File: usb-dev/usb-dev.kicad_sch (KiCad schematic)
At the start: 42 parts, among them J1 HS USB, J2 FS USB, J3 Conn_02x05_Odd_Even, J4 Conn_02x05_Odd_Even, J5 Molex_104031-0811, J6 Conn_01x06_Male, SW1 SW_Push, SW2 SW_Push, SW3 SW_Push, U1 LPC55x16JEV98E, U2 AP2127K-3.3, Y1 ABM8-16.000MHZ-B2-T

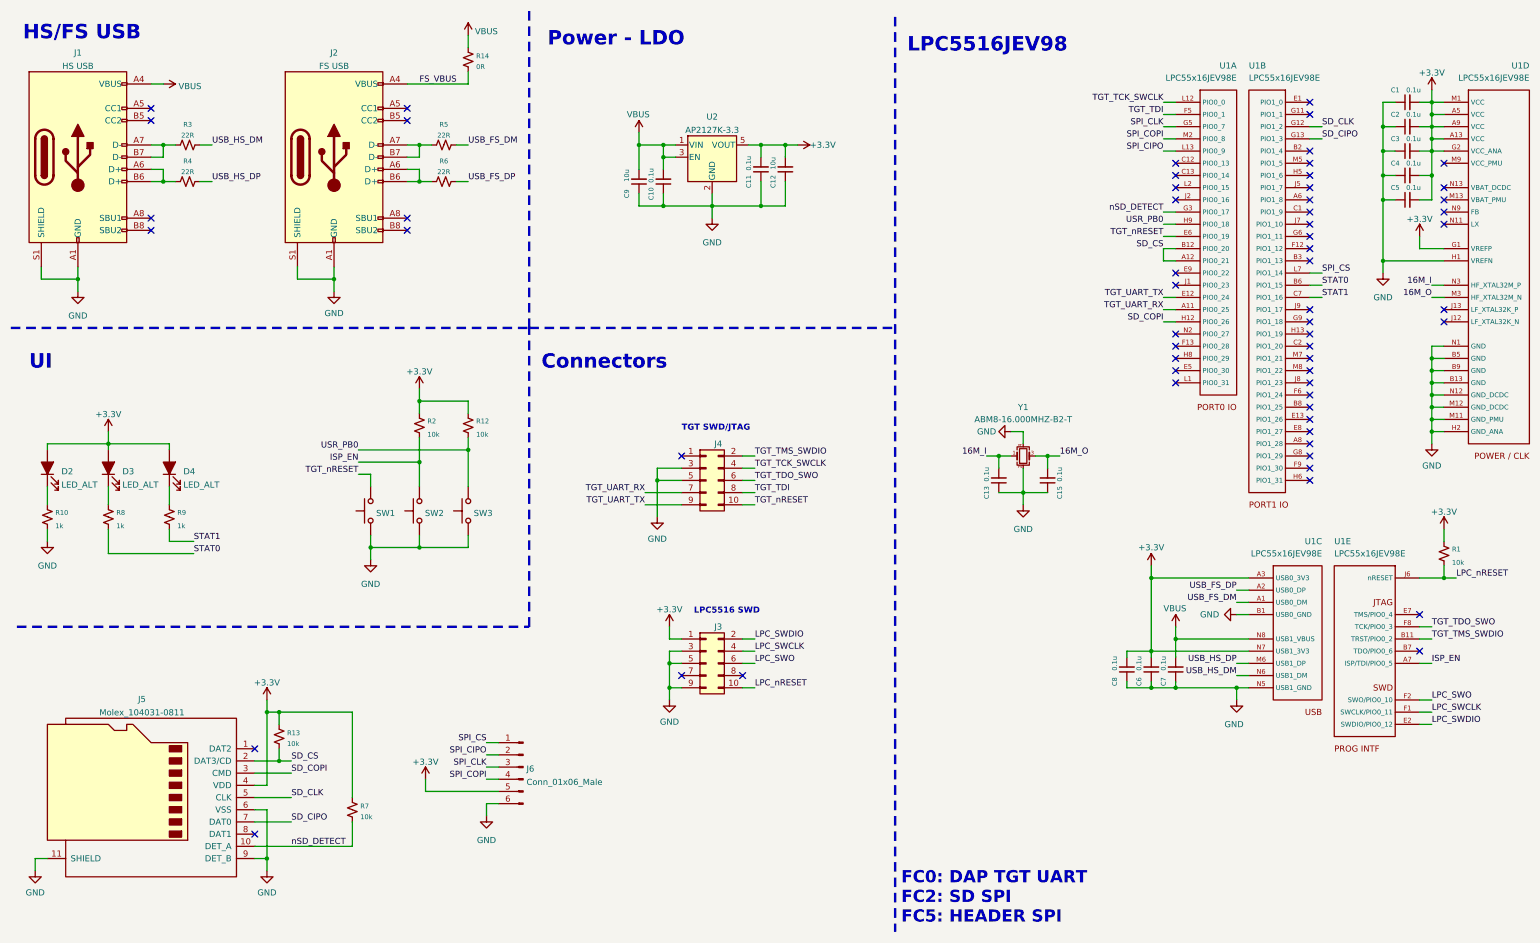
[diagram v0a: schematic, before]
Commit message: Fixed VDD_PMU, added fet to SD power and added extra CS line to SPI header
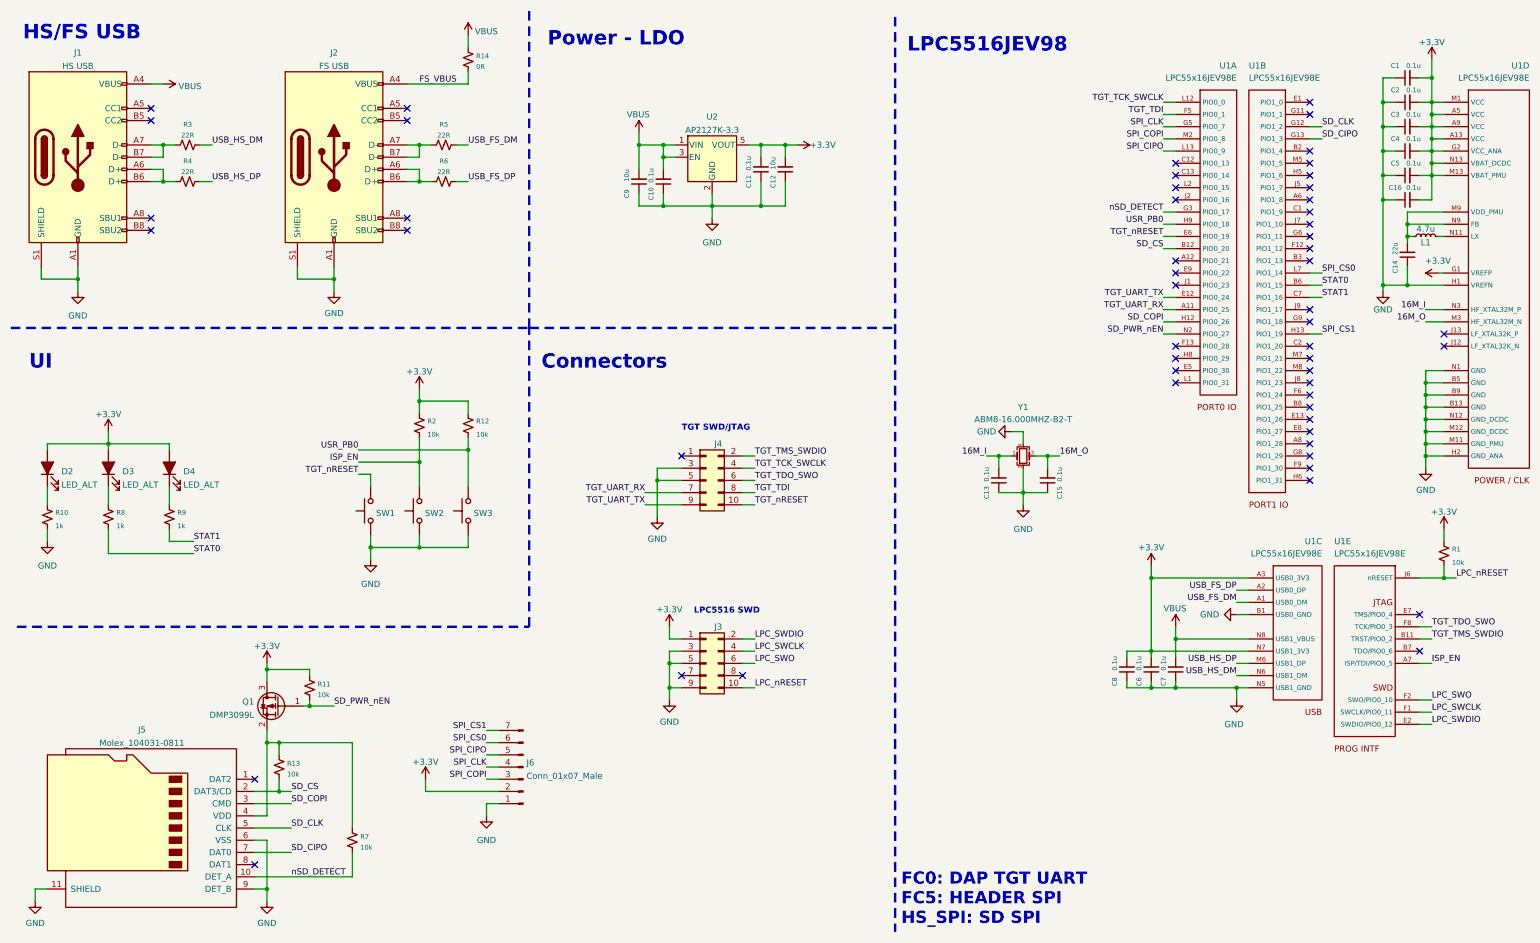
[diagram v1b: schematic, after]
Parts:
- removed J6: Conn_01x06_Male, Connector_PinHeader_2.54mm:PinHeader_1x06_P2.54mm_Vertical, symbol Connector:Conn_01x06_Male
- added C14: 22u, Capacitor_SMD:C_0402_1005Metric, symbol Device:C_Small
- added C16: 0.1u, Capacitor_SMD:C_0402_1005Metric, symbol Device:C_Small
- added J6: Conn_01x07_Male, Connector_PinHeader_2.54mm:PinHeader_1x07_P2.54mm_Vertical, symbol Connector:Conn_01x07_Male
- added L1: 4.7u, Inductor_SMD:L_0805_2012Metric, symbol Device:L_Small
- added Q1: DMP3099L, Package_TO_SOT_SMD:SOT-23, symbol Device:Q_PMOS_GSD
- added R11: 10k, Resistor_SMD:R_0402_1005Metric, symbol Device:R_Small_US
- J3, J4: footprint Connector_PinHeader_1.00mm:PinHeader_2x05_P1.00mm_Vertical_SMD -> Connector_PinHeader_1.27mm:PinHeader_2x05_P1.27mm_Vertical_SMD
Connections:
- net +3V3: now also U1.M13 (VBAT_PMU), U1.N13 (VBAT_DCDC), C16.2, J6.2 (Pin_2), Q1.3 (D), R11.2; no longer J5.4 (VDD), R13.2, R7.2
- net GND: now also C14.1, C16.1, J6.1 (Pin_1)
- net SD_CS: no longer U1.A12 (PIO0_21)
- net SPI_CIPO: now also J6.5 (Pin_5)
- net SPI_CLK: now also J6.4 (Pin_4)
- net SPI_COPI: now also J6.3 (Pin_3)
- net SD_PWR_nEN: now reaches U1.N2 (PIO0_27)
- net SD_PWR_nEN: now also Q1.1 (G), R11.1
- net at U1.M9 (VDD_PMU): now also U1.N9 (FB), C14.2, L1.1
- net at U1.N11 (LX): now also L1.2
- net SPI_CS1: now reaches U1.H13 (PIO1_19)
- net SPI_CS1: now also J6.7 (Pin_7)
- net SPI_CS renamed SPI_CS0
- net SPI_CS0: now also J6.6 (Pin_6)
- new net: J5.4 (VDD), Q1.2 (S), R13.2, R7.2
- no-connect marks 60 -> 54
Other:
- note added: "FC0: DAP TGT UART FC5: HEADER SPI HS_SPI: SD SPI"
- note removed: "FC0: DAP TGT UART FC2: SD SPI FC5: HEADER SPI"
- moved on the sheet: C1, C2, C3, C4, C5, J5, R13, R7, U1D

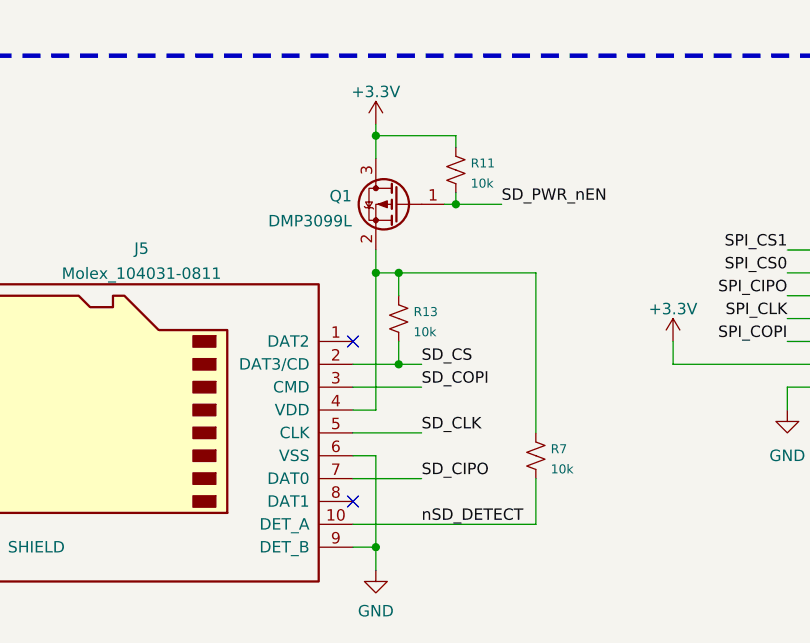
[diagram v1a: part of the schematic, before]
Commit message: Fixed missing VDDCORE connections to internal switcher D:
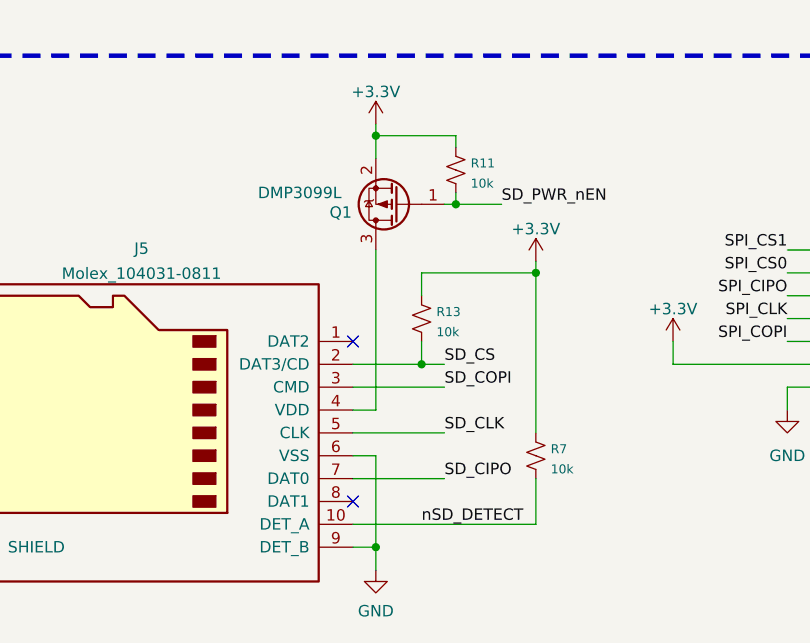
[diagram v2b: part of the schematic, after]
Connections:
- net +3V3: now also Q1.2 (S), R13.2, R7.2; no longer Q1.3 (D)
- new net: J5.4 (VDD), Q1.3 (D)
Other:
- moved on the sheet: Q1, R13
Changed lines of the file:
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@@
   (junction (at 43.18 39.37) (diameter 0) (color 0 0 0 0)
   )
-  (junction (at 67.31 163.83) (diameter 0) (color 0 0 0 0)
-  )
   (junction (at 157.48 52.07) (diameter 0) (color 0 0 0 0)
   )
@@
   (junction (at 222.25 111.76) (diameter 0) (color 0 0 0 0)
   )
-  (junction (at 67.31 173.99) (diameter 0) (color 0 0 0 0)
+  (junction (at 69.85 173.99) (diameter 0) (color 0 0 0 0)
   )
   (junction (at 106.68 102.87) (diameter 0) (color 0 0 0 0)
   )
+  (junction (at 64.77 148.59) (diameter 0) (color 0 0 0 0)
+  )
   (junction (at 148.59 152.4) (diameter 0) (color 0 0 0 0)
   )
   (junction (at 96.52 92.71) (diameter 0) (color 0 0 0 0)
   )
+  (junction (at 73.66 156.21) (diameter 0) (color 0 0 0 0)
+  )
   (junction (at 25.4 67.31) (diameter 0) (color 0 0 0 0)
   )
@@
   (junction (at 307.34 35.56) (diameter 0) (color 0 0 0 0)
   )
-  (junction (at 64.77 148.59) (diameter 0) (color 0 0 0 0)
-  )
   (junction (at 146.05 109.22) (diameter 0) (color 0 0 0 0)
   )
@@
   (junction (at 297.18 40.64) (diameter 0) (color 0 0 0 0)
   )
+  (junction (at 82.55 163.83) (diameter 0) (color 0 0 0 0)
+  )
   (junction (at 307.34 40.64) (diameter 0) (color 0 0 0 0)
   )
   (junction (at 227.33 104.14) (diameter 0) (color 0 0 0 0)
   )
-  (junction (at 64.77 163.83) (diameter 0) (color 0 0 0 0)
-  )
   (junction (at 96.52 46.99) (diameter 0) (color 0 0 0 0)
   )
@@
   )
   (junction (at 307.34 30.48) (diameter 0) (color 0 0 0 0)
-  )
-  (junction (at 73.66 156.21) (diameter 0) (color 0 0 0 0)
   )
   (junction (at 248.92 129.54) (diameter 0) (color 0 0 0 0)
@@
   (no_connect (at 62.23 189.23))
   (no_connect (at 163.83 149.86))
-  (wire (pts (xy 67.31 173.99) (xy 69.85 173.99))
+  (wire (pts (xy 69.85 173.99) (xy 72.39 173.99))
     (stroke (width 0) (type default) (color 0 0 0 0))
   )
@@
     (stroke (width 0) (type default) (color 0 0 0 0))
   )
-  (wire (pts (xy 67.31 163.83) (xy 64.77 163.83))
-    (stroke (width 0) (type default) (color 0 0 0 0))
-  )
   (wire (pts (xy 307.34 45.72) (xy 307.34 43.18))
     (stroke (width 0) (type default) (color 0 0 0 0))
@@
     (stroke (width 0.5) (type dash_dot) (color 0 0 0 0))
   )
+  (wire (pts (xy 82.55 162.56) (xy 82.55 163.83))
+    (stroke (width 0) (type default) (color 0 0 0 0))
+  )
   (wire (pts (xy 157.48 49.53) (xy 157.48 52.07))
     (stroke (width 0) (type default) (color 0 0 0 0))
@@
     (stroke (width 0) (type default) (color 0 0 0 0))
   )
-  (wire (pts (xy 67.31 163.83) (xy 82.55 163.83))
+  (wire (pts (xy 69.85 163.83) (xy 82.55 163.83))
     (stroke (width 0) (type default) (color 0 0 0 0))
   )
@@
   )
   (wire (pts (xy 302.26 68.58) (xy 297.18 68.58))
+    (stroke (width 0) (type default) (color 0 0 0 0))
+  )
+  (wire (pts (xy 72.39 156.21) (xy 73.66 156.21))
     (stroke (width 0) (type default) (color 0 0 0 0))
   )
@@
     (stroke (width 0) (type default) (color 0 0 0 0))
   )
-  (wire (pts (xy 67.31 171.45) (xy 67.31 173.99))
+  (wire (pts (xy 69.85 171.45) (xy 69.85 173.99))
     (stroke (width 0) (type default) (color 0 0 0 0))
   )
@@
   )
   (wire (pts (xy 304.8 45.72) (xy 307.34 45.72))
-    (stroke (width 0) (type default) (color 0 0 0 0))
-  )
-  (wire (pts (xy 64.77 161.29) (xy 64.77 163.83))
     (stroke (width 0) (type default) (color 0 0 0 0))
   )
@@
     (stroke (width 0) (type default) (color 0 0 0 0))
   )
+  (wire (pts (xy 64.77 148.59) (xy 64.77 151.13))
+    (stroke (width 0) (type default) (color 0 0 0 0))
+  )
   (wire (pts (xy 64.77 148.59) (xy 73.66 148.59))
     (stroke (width 0) (type default) (color 0 0 0 0))
   )
   (wire (pts (xy 104.14 39.37) (xy 106.68 39.37))
-    (stroke (width 0) (type default) (color 0 0 0 0))
-  )
-  (wire (pts (xy 72.39 156.21) (xy 73.66 156.21))
     (stroke (width 0) (type default) (color 0 0 0 0))
   )
@@
     (stroke (width 0) (type default) (color 0 0 0 0))
   )
-  (wire (pts (xy 62.23 186.69) (xy 69.85 186.69))
+  (wire (pts (xy 62.23 186.69) (xy 72.39 186.69))
     (stroke (width 0) (type default) (color 0 0 0 0))
   )
@@
     (stroke (width 0) (type default) (color 0 0 0 0))
   )
-  (wire (pts (xy 64.77 148.59) (xy 64.77 151.13))
-    (stroke (width 0) (type default) (color 0 0 0 0))
-  )
   (wire (pts (xy 96.52 92.71) (xy 106.68 92.71))
     (stroke (width 0) (type default) (color 0 0 0 0))
@@
     (stroke (width 0) (type default) (color 0 0 0 0))
   )
-  (wire (pts (xy 64.77 163.83) (xy 64.77 179.07))
-    (stroke (width 0) (type default) (color 0 0 0 0))
-  )
   (wire (pts (xy 243.84 151.13) (xy 243.84 152.4))
     (stroke (width 0) (type default) (color 0 0 0 0))
@@
     (stroke (width 0) (type default) (color 0 0 0 0))
   )
-  (wire (pts (xy 67.31 166.37) (xy 67.31 163.83))
+  (wire (pts (xy 69.85 166.37) (xy 69.85 163.83))
     (stroke (width 0) (type default) (color 0 0 0 0))
   )
@@
     (stroke (width 0) (type default) (color 0 0 0 0))
   )
+  (wire (pts (xy 64.77 161.29) (xy 64.77 179.07))
+    (stroke (width 0) (type default) (color 0 0 0 0))
+  )
   (wire (pts (xy 307.34 33.02) (xy 309.88 33.02))
     (stroke (width 0) (type default) (color 0 0 0 0))
@@
     (stroke (width 0) (type default) (color 0 0 0 0))
   )
-  (wire (pts (xy 62.23 176.53) (xy 69.85 176.53))
+  (wire (pts (xy 62.23 176.53) (xy 72.39 176.53))
     (stroke (width 0) (type default) (color 0 0 0 0))
   )
@@
     (stroke (width 0) (type default) (color 0 0 0 0))
   )
-  (wire (pts (xy 62.23 173.99) (xy 67.31 173.99))
+  (wire (pts (xy 62.23 173.99) (xy 69.85 173.99))
     (stroke (width 0) (type default) (color 0 0 0 0))
   )
@@
     (stroke (width 0) (type default) (color 0 0 0 0))
   )
-  (wire (pts (xy 62.23 181.61) (xy 69.85 181.61))
+  (wire (pts (xy 62.23 181.61) (xy 72.39 181.61))
     (stroke (width 0) (type default) (color 0 0 0 0))
   )
@@
     (effects (font (size 1.27 1.27)) (justify left bottom))
   )
-  (label "SD_CIPO" (at 69.85 186.69 0)
+  (label "SD_CIPO" (at 72.39 186.69 0)
     (effects (font (size 1.27 1.27)) (justify left bottom))
   )
@@
     (effects (font (size 1.27 1.27)) (justify right bottom))
   )
-  (label "SD_CS" (at 69.85 173.99 0)
+  (label "SD_CS" (at 72.39 173.99 0)
     (effects (font (size 1.27 1.27)) (justify left bottom))
   )
@@
     (effects (font (size 1.27 1.27)) (justify right bottom))
   )
-  (label "SD_COPI" (at 69.85 176.53 0)
-    (effects (font (size 1.27 1.27)) (justify left bottom))
-  )
-  (label "SD_CLK" (at 69.85 181.61 0)
+  (label "SD_COPI" (at 72.39 176.53 0)
+    (effects (font (size 1.27 1.27)) (justify left bottom))
+  )
+  (label "SD_CLK" (at 72.39 181.61 0)
     (effects (font (size 1.27 1.27)) (justify left bottom))
   )
@@
     (pin "2")
   )
-  (symbol (lib_id "Device:R_Small_US") (at 67.31 168.91 180) (unit 1)
-    (in_bom yes) (on_board yes) (fields_autoplaced)
-    (property "Reference" "R13" (id 0) (at 68.961 168.1677 0)
+  (symbol (lib_id "Device:R_Small_US") (at 69.85 168.91 180) (unit 1)
+    (in_bom yes) (on_board yes) (fields_autoplaced)
+    (property "Reference" "R13" (id 0) (at 71.501 168.1677 0)
       (effects (font (size 1 1)) (justify right))
     )
-    (property "Value" "10k" (id 1) (at 68.961 170.4067 0)
+    (property "Value" "10k" (id 1) (at 71.501 170.4067 0)
       (effects (font (size 1 1)) (justify right))
     )
-    (property "Footprint" "Resistor_SMD:R_0402_1005Metric" (id 2) (at 67.31 168.91 0)
-      (effects (font (size 1.27 1.27)) hide)
-    )
-    (property "Datasheet" "~" (id 3) (at 67.31 168.91 0)
+    (property "Footprint" "Resistor_SMD:R_0402_1005Metric" (id 2) (at 69.85 168.91 0)
+      (effects (font (size 1.27 1.27)) hide)
+    )
+    (property "Datasheet" "~" (id 3) (at 69.85 168.91 0)
       (effects (font (size 1.27 1.27)) hide)
     )
@@
     (pin "2")
   )
-  (symbol (lib_id "Device:Q_PMOS_GSD") (at 67.31 156.21 0) (mirror y) (unit 1)
-    (in_bom yes) (on_board yes) (fields_autoplaced)
-    (property "Reference" "Q1" (id 0) (at 62.1031 155.3015 0)
+  (symbol (lib_id "Device:Q_PMOS_GSD") (at 67.31 156.21 180) (unit 1)
+    (in_bom yes) (on_board yes)
+    (property "Reference" "Q1" (id 0) (at 62.1031 157.1185 0)
       (effects (font (size 1.27 1.27)) (justify left))
     )
-    (property "Value" "DMP3099L" (id 1) (at 62.1031 158.0766 0)
+    (property "Value" "DMP3099L" (id 1) (at 60.96 154.94 0)
       (effects (font (size 1.27 1.27)) (justify left))
     )
-    (property "Footprint" "Package_TO_SOT_SMD:SOT-23" (id 2) (at 62.23 153.67 0)
+    (property "Footprint" "Package_TO_SOT_SMD:SOT-23" (id 2) (at 62.23 158.75 0)
       (effects (font (size 1.27 1.27)) hide)
     )
@@
     (pin "1")
     (pin "2")
+  )
+  (symbol (lib_id "power:+3.3V") (at 82.55 162.56 0) (unit 1)
+    (in_bom yes) (on_board yes) (fields_autoplaced)
+    (property "Reference" "#PWR0105" (id 0) (at 82.55 166.37 0)
+      (effects (font (size 1.27 1.27)) hide)
+    )
+    (property "Value" "+3.3V" (id 1) (at 82.55 158.9555 0))
+    (property "Footprint" "" (id 2) (at 82.55 162.56 0)
+      (effects (font (size 1.27 1.27)) hide)
+    )
+    (property "Datasheet" "" (id 3) (at 82.55 162.56 0)
+      (effects (font (size 1.27 1.27)) hide)
+    )
+    (pin "1")
   )
   (sheet_instances
@@
       (reference "#PWR0104") (unit 1) (value "+3.3V") (footprint "")
     )
+    (path "/fa7db4f9-3398-4772-8fa3-435b9044520a"
+      (reference "#PWR0105") (unit 1) (value "+3.3V") (footprint "")
+    )
     (path "/09298748-d31e-4599-986f-caa3b45b4a82"
